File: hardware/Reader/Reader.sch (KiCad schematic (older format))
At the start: 0 parts

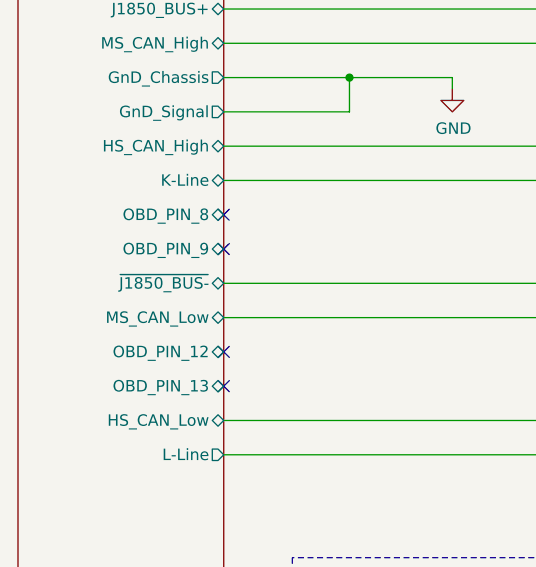
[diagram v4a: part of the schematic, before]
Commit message: Fixed bugs on the reader schematic. Exported Schematic Electrical report
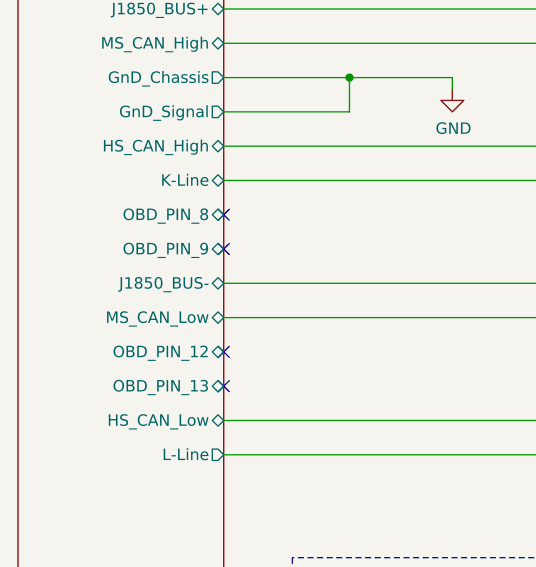
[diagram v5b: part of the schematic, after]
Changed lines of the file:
@@
 F10 "OBD_PIN_8" B R 1600 2450 50
 F11 "OBD_PIN_9" B R 1600 2600 50
-F12 "~J1850_BUS-~" B R 1600 2750 50
-F13 "MS_CAN_Low" B R 1600 2900 50
-F14 "OBD_PIN_12" B R 1600 3050 50
-F15 "OBD_PIN_13" B R 1600 3200 50
-F16 "HS_CAN_Low" B R 1600 3350 50
-F17 "L-Line" O R 1600 3500 50
+F12 "MS_CAN_Low" B R 1600 2900 50
+F13 "OBD_PIN_12" B R 1600 3050 50
+F14 "OBD_PIN_13" B R 1600 3200 50
+F15 "HS_CAN_Low" B R 1600 3350 50
+F16 "L-Line" O R 1600 3500 50
+F17 "J1850_BUS-" B R 1600 2750 50
 $EndSheet
 Wire Wire Line

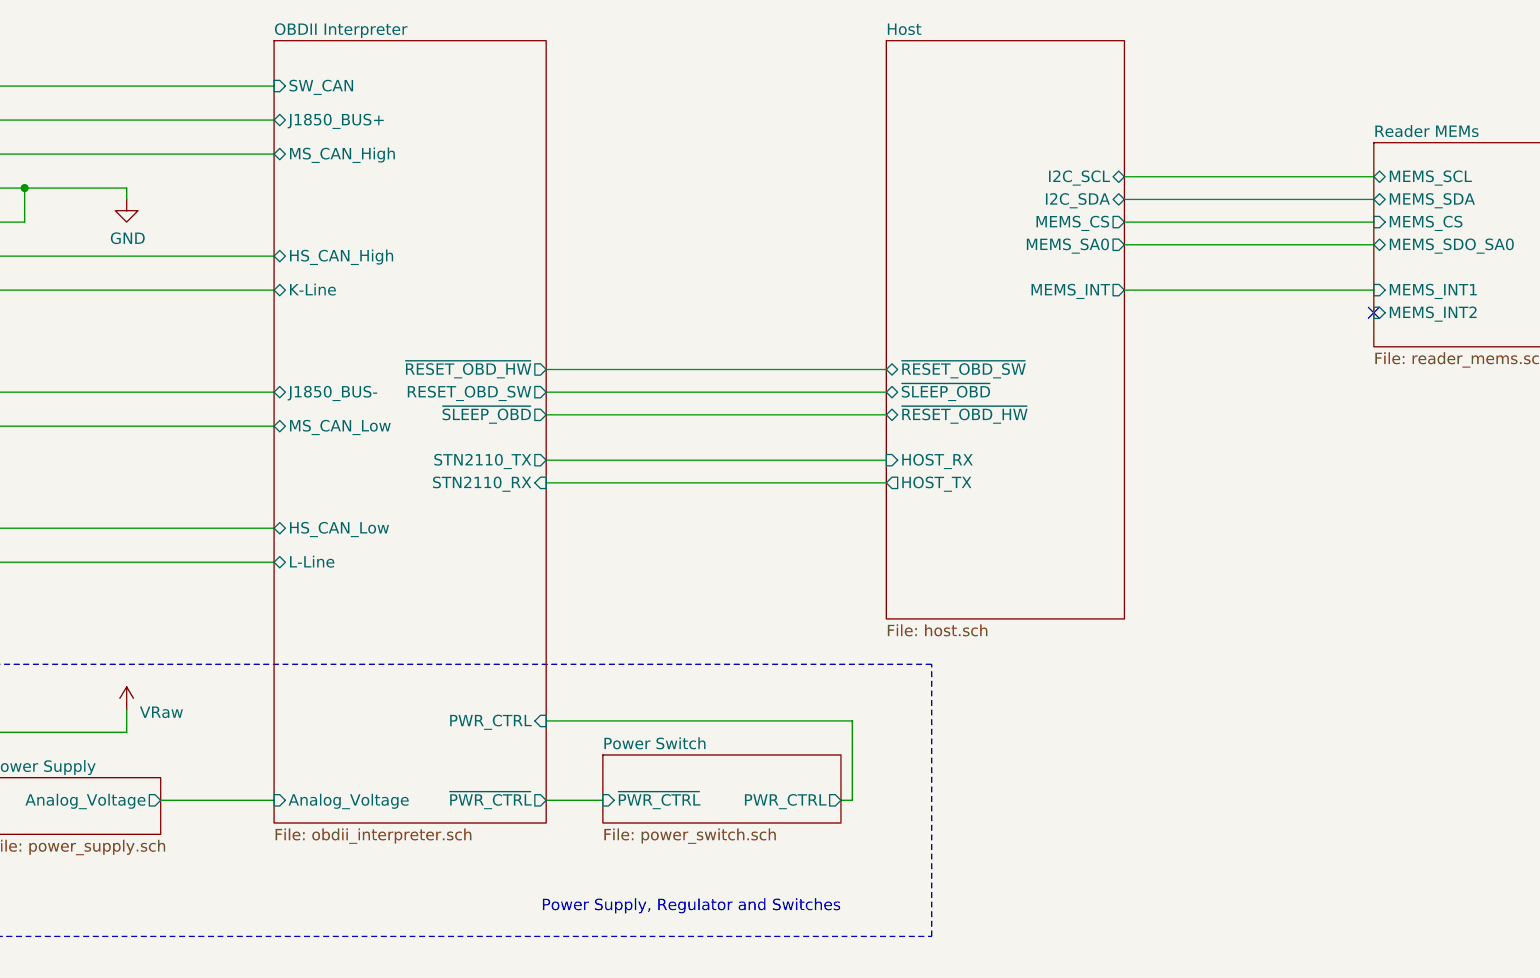
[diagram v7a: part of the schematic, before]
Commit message: Fixed bugs in schematic. Updated BOM list. Swapped to using ESP32 holder. Updated PCB layout to v0.0.2. Updated schematic to v0.0.4
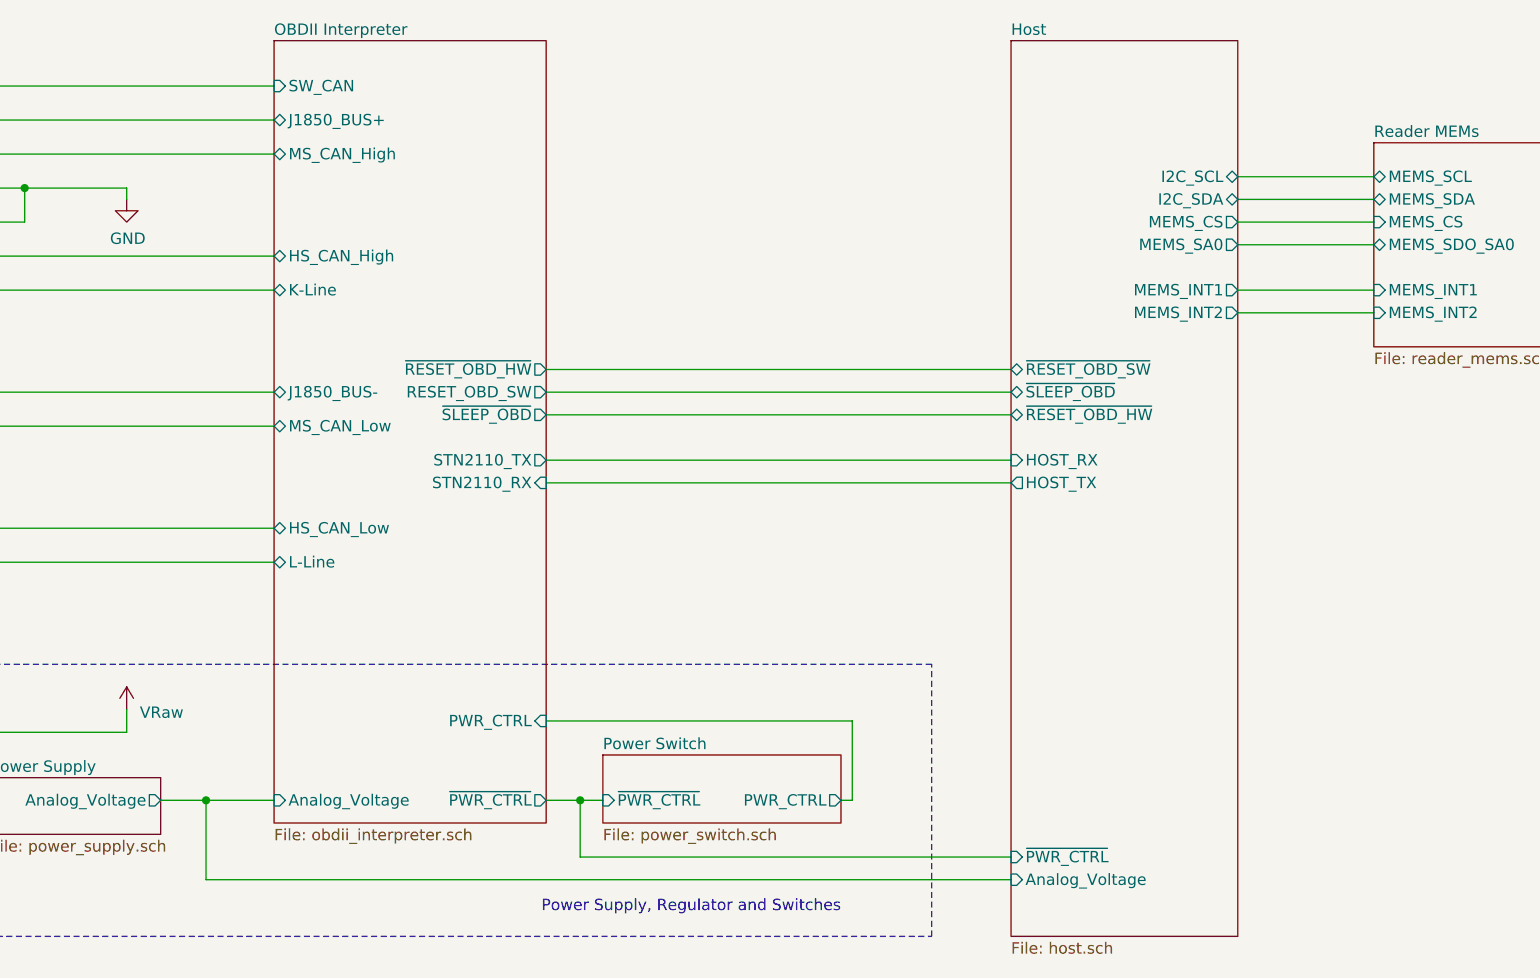
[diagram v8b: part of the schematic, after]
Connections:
- no-connect marks 5 -> 4
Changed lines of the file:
@@
 Sheet 1 19
 Title "CANnect Reader"
-Date "2020-10-27"
-Rev "0.0.03"
+Date "2020-10-28"
+Rev "0.0.04"
 Comp "CANtech"
 Comment1 "Created by Choong Jin Ng | jin8383@gmail.com"
@@
 	2600 4250 2600 4150
 Wire Wire Line
-	2750 4550 3250 4550
+	2750 4550 2950 4550
 $Sheet
 S 3250 1200 1200 3450
@@
 NoConn ~ 1600 3200
 Wire Wire Line
-	4450 4550 4700 4550
+	4450 4550 4600 4550
 Wire Wire Line
 	5750 4550 5800 4550
@@
 	1600 3350 3250 3350
 Wire Wire Line
-	5950 2650 4450 2650
-Wire Wire Line
-	4450 2750 5950 2750
-Wire Wire Line
-	5950 2850 4450 2850
-Wire Wire Line
-	8100 2300 7000 2300
-Wire Wire Line
-	7000 2100 8100 2100
-Wire Wire Line
-	7000 1800 8100 1800
-Wire Wire Line
-	5950 3150 4450 3150
-Wire Wire Line
-	4450 3050 5950 3050
-$Sheet
-S 5950 1200 1050 2550
+	6500 2650 4450 2650
+Wire Wire Line
+	4450 2750 6500 2750
+Wire Wire Line
+	6500 2850 4450 2850
+Wire Wire Line
+	6500 3150 4450 3150
+Wire Wire Line
+	4450 3050 6500 3050
+$Sheet
+S 6500 1200 1000 3950
 U 5F91C7D3
 F0 "Host" 50
 F1 "host.sch" 50
-F2 "HOST_RX" I L 5950 3050 50
-F3 "HOST_TX" O L 5950 3150 50
-F4 "I2C_SCL" B R 7000 1800 50
-F5 "I2C_SDA" B R 7000 1900 50
-F6 "MEMS_INT" O R 7000 2300 50
-F7 "~SLEEP_OBD~" B L 5950 2750 50
-F8 "~RESET_OBD_SW~" B L 5950 2650 50
-F9 "~RESET_OBD_HW~" B L 5950 2850 50
-F10 "MEMS_CS" O R 7000 2000 50
-F11 "MEMS_SA0" O R 7000 2100 50
-$EndSheet
-NoConn ~ 8100 2400
-Wire Wire Line
-	7000 1900 8100 1900
-Wire Wire Line
-	7000 2000 8100 2000
+F2 "HOST_RX" I L 6500 3050 50
+F3 "HOST_TX" O L 6500 3150 50
+F4 "I2C_SCL" B R 7500 1800 50
+F5 "I2C_SDA" B R 7500 1900 50
+F6 "~SLEEP_OBD~" B L 6500 2750 50
+F7 "~RESET_OBD_SW~" B L 6500 2650 50
+F8 "~RESET_OBD_HW~" B L 6500 2850 50
+F9 "MEMS_CS" O R 7500 2000 50
+F10 "MEMS_SA0" O R 7500 2100 50
+F11 "Analog_Voltage" I L 6500 4900 50
+F12 "~PWR_CTRL~" I L 6500 4800 50
+F13 "MEMS_INT2" O R 7500 2400 50
+F14 "MEMS_INT1" O R 7500 2300 50
+$EndSheet
 $Sheet
 S 8100 1650 850  900
@@
 F2 "Analog_Voltage" O R 2750 4550 50
 $EndSheet
+Wire Wire Line
+	2950 4550 2950 4900
+Wire Wire Line
+	2950 4900 6500 4900
+Connection ~ 2950 4550
+Wire Wire Line
+	2950 4550 3250 4550
+Wire Wire Line
+	4600 4550 4600 4800
+Wire Wire Line
+	4600 4800 6500 4800
+Connection ~ 4600 4550
+Wire Wire Line
+	4600 4550 4700 4550
+Wire Wire Line
+	7500 1800 8100 1800
+Wire Wire Line
+	7500 1900 8100 1900
+Wire Wire Line
+	7500 2000 8100 2000
+Wire Wire Line
+	7500 2100 8100 2100
+Wire Wire Line
+	7500 2300 8100 2300
+Wire Wire Line
+	8100 2400 7500 2400
 $EndSCHEMATC
